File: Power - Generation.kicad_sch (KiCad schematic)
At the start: 34 parts, among them Q1 AO3400A, Q2 AO3400A, Q3 SI2301CDS-T1-GE3, SW8 Button SPST SMD Tactile Switch, U4 AMS1117-3.3, U5 TPS61252DSG

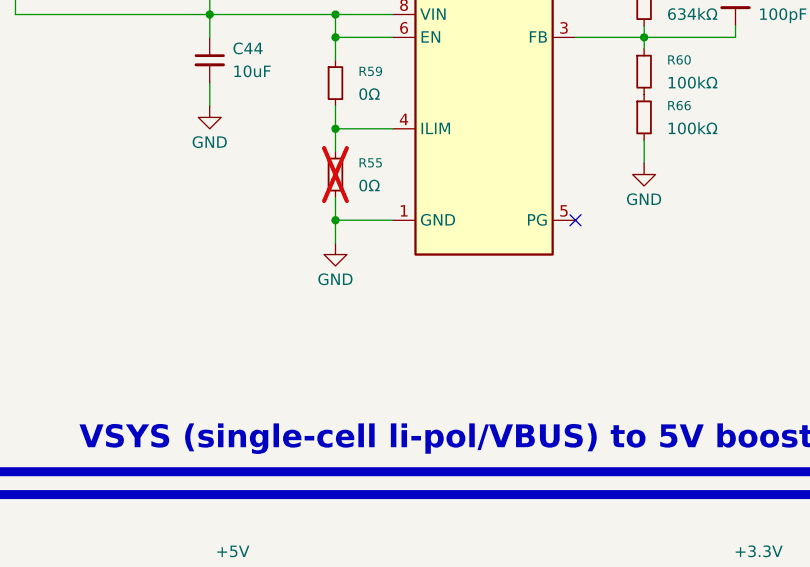
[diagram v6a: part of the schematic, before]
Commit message: routing zasilania caly czas + polygony masy, lekkie zmienienie layoutu - chyba dążenie do zmniejszenia wymiarow plytki - moze 100x100mm?
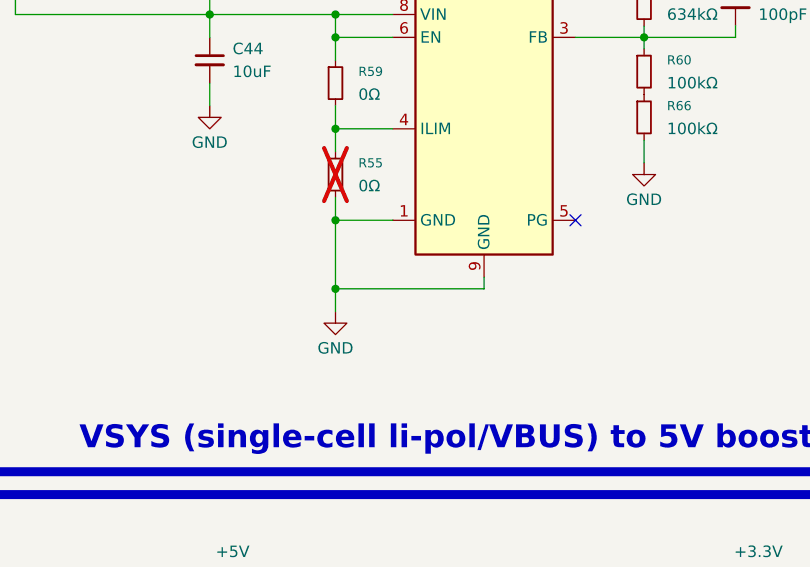
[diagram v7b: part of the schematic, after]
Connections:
- net GND: now also U5.9 (GND)
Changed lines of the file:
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@@
 	)
 	(junction
+		(at 232.41 129.54)
+		(diameter 0)
+		(color 0 0 0 0)
+	)
+	(junction
 		(at 168.91 99.06)
 		(diameter 0)
@@
 	(wire
 		(pts
-			(xy 232.41 121.92) (xy 232.41 124.46)
+			(xy 232.41 121.92) (xy 232.41 129.54)
 		)
 		(stroke
@@
 	(wire
 		(pts
+			(xy 248.92 128.27) (xy 248.92 129.54)
+		)
+		(stroke
+			(width 0)
+			(type default)
+		)
+	)
+	(wire
+		(pts
 			(xy 152.4 129.54) (xy 158.75 129.54)
 		)
@@
 	(wire
 		(pts
+			(xy 232.41 129.54) (xy 248.92 129.54)
+		)
+		(stroke
+			(width 0)
+			(type default)
+		)
+	)
+	(wire
+		(pts
 			(xy 105.41 163.83) (xy 105.41 168.91)
 		)
@@
 	(wire
 		(pts
+			(xy 232.41 129.54) (xy 232.41 132.08)
+		)
+		(stroke
+			(width 0)
+			(type default)
+		)
+	)
+	(wire
+		(pts
 			(xy 130.81 99.06) (xy 139.7 99.06)
 		)
@@
 	(symbol
 		(lib_id "power:GND")
-		(at 232.41 124.46 0)
+		(at 232.41 132.08 0)
+		(mirror y)
 		(unit 1)
 		(exclude_from_sim no)
@@
 		(dnp no)
 		(property "Reference" "#PWR0107"
-			(at 232.41 130.81 0)
+			(at 232.41 138.43 0)
 			(effects
 				(font
@@
 		)
 		(property "Value" "GND"
-			(at 232.41 128.524 0)
+			(at 232.41 136.144 0)
 			(effects
 				(font
@@
 		)
 		(property "Footprint" ""
-			(at 232.41 124.46 0)
+			(at 232.41 132.08 0)
 			(effects
 				(font
@@
 		)
 		(property "Datasheet" ""
-			(at 232.41 124.46 0)
+			(at 232.41 132.08 0)
 			(effects
 				(font
@@
 		)
 		(property "Description" "Power symbol creates a global label with name \"GND\" , ground"
-			(at 232.41 124.46 0)
+			(at 232.41 132.08 0)
 			(effects
 				(font
